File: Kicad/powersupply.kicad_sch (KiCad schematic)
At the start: 26 parts, among them J1101 Jack 2.1{slash}6.3mm, J1102 Conn_02x02, J1103 Conn_01x04, Q1101 SS8050, Q1102 AO3401A, Q1103 SS8550, U1101 DC-DC Module, U1102 LP2950N, U1103 AMS1117-3.3

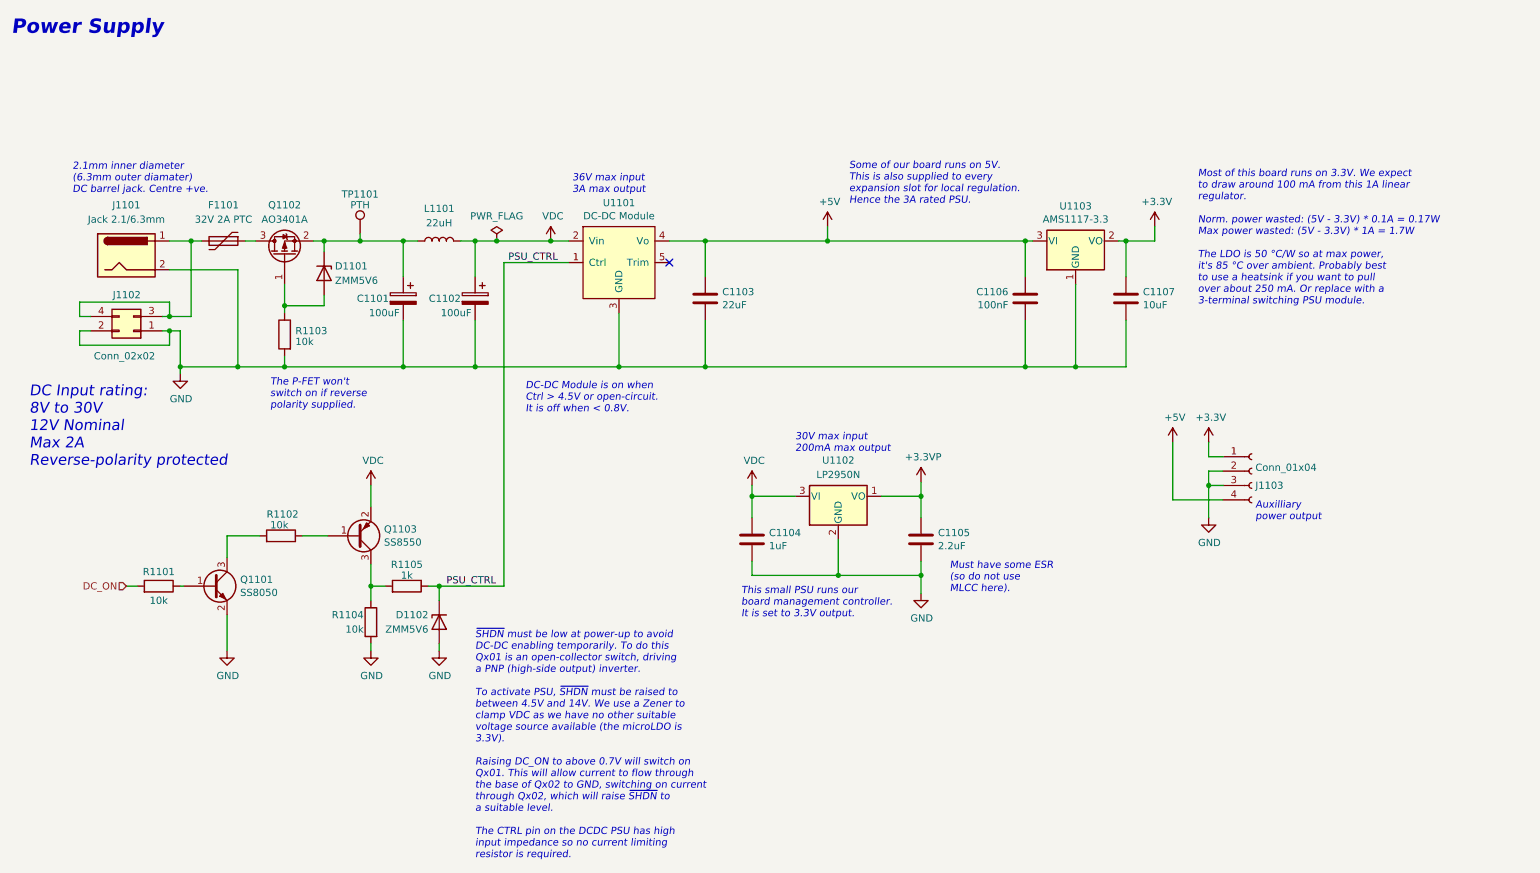
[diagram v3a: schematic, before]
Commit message: Reworked audio circuit.
Based on TLV320AIC23B evaluation board. Removed Pi filters. Used SMD
electrolytic caps for headphone out.
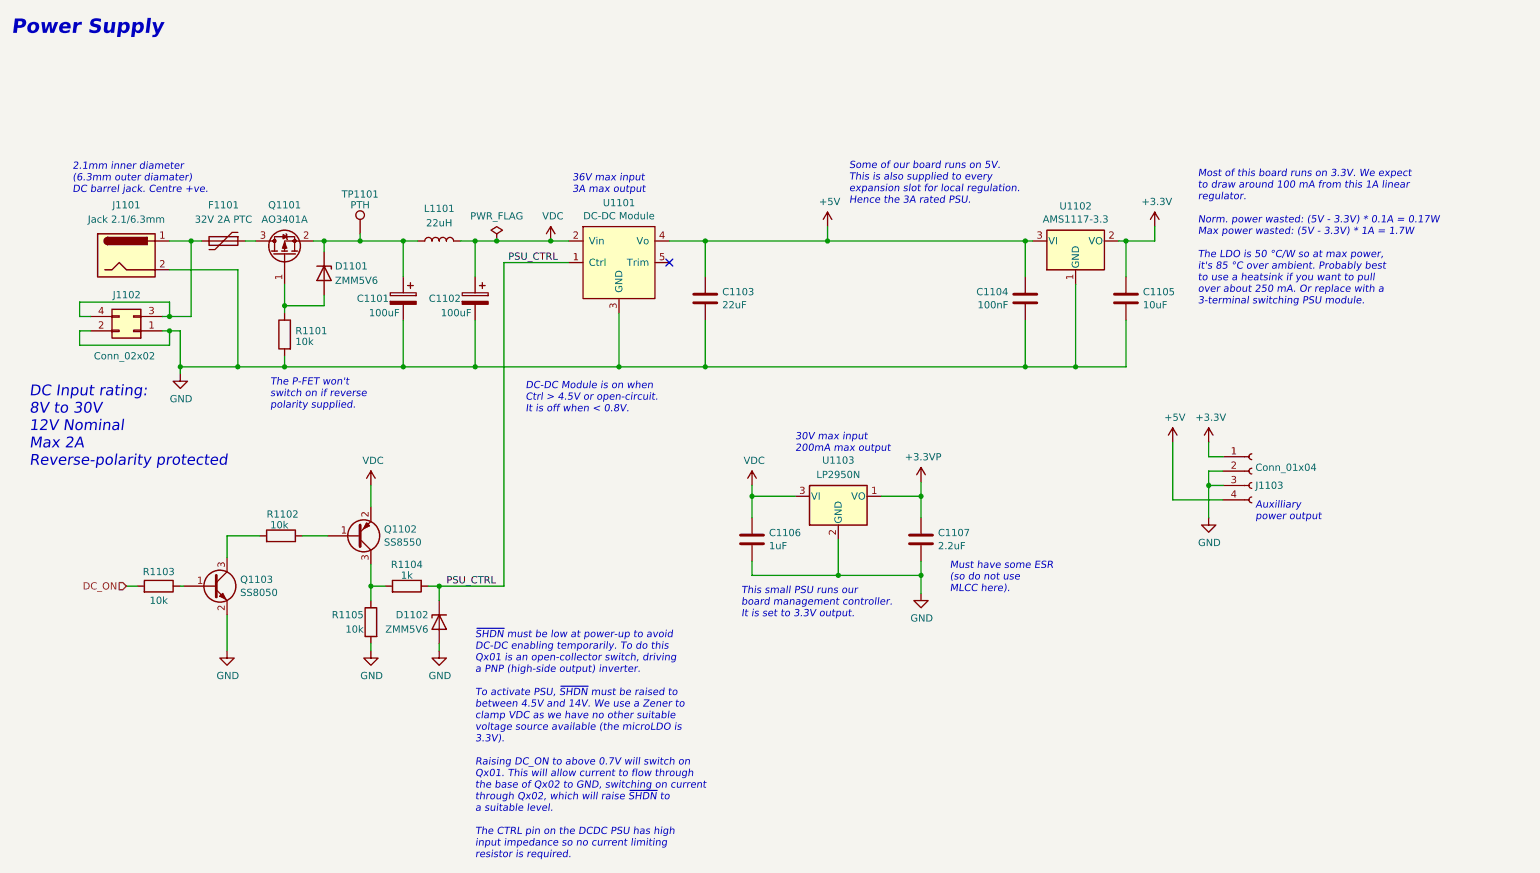
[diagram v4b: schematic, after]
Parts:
- renumbered C1106 to C1104, C1107 to C1105, C1104 to C1106, C1105 to C1107, Q1102 to Q1101, Q1103 to Q1102, Q1101 to Q1103, R1103 to R1101, R1101 to R1103, R1105 to R1104, R1104 to R1105, U1103 to U1102, U1102 to U1103
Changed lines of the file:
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@@
   (symbol (lib_id "Regulator_Linear:AMS1117CD-3.3") (at 200.66 53.975 0) (unit 1)
     (in_bom yes) (on_board yes)
-    (property "Reference" "U1103" (id 0) (at 200.66 47.8282 0))
+    (property "Reference" "U1102" (id 0) (at 200.66 47.8282 0))
     (property "Value" "AMS1117-3.3" (id 1) (at 200.66 50.1396 0))
     (property "Footprint" "Package_TO_SOT_SMD:SOT-223-3_TabPin2" (id 2) (at 200.66 48.895 0)
@@
   (symbol (lib_id "power:GND") (at 42.545 77.47 0) (unit 1)
     (in_bom yes) (on_board yes)
-    (property "Reference" "#PWR01101" (id 0) (at 42.545 83.82 0)
+    (property "Reference" "#PWR01104" (id 0) (at 42.545 83.82 0)
       (effects (font (size 1.27 1.27)) hide)
     )
@@
   (symbol (lib_id "power:+3.3VP") (at 173.355 96.52 0) (unit 1)
     (in_bom yes) (on_board yes)
-    (property "Reference" "#PWR01109" (id 0) (at 177.165 97.79 0)
+    (property "Reference" "#PWR01107" (id 0) (at 177.165 97.79 0)
       (effects (font (size 1.27 1.27)) hide)
     )
@@
   (symbol (lib_id "power:+3.3V") (at 214.63 51.435 0) (unit 1)
     (in_bom yes) (on_board yes)
-    (property "Reference" "#PWR01111" (id 0) (at 214.63 55.245 0)
+    (property "Reference" "#PWR01102" (id 0) (at 214.63 55.245 0)
       (effects (font (size 1.27 1.27)) hide)
     )
@@
   (symbol (lib_id "Device:C") (at 191.77 64.135 0) (mirror y) (unit 1)
     (in_bom yes) (on_board yes)
-    (property "Reference" "C1106" (id 0) (at 188.7728 62.9666 0)
+    (property "Reference" "C1104" (id 0) (at 188.7728 62.9666 0)
       (effects (font (size 1.27 1.27)) (justify left))
     )
@@
   (symbol (lib_id "power:GND") (at 173.355 116.205 0) (unit 1)
     (in_bom yes) (on_board yes)
-    (property "Reference" "#PWR01110" (id 0) (at 173.355 122.555 0)
+    (property "Reference" "#PWR01111" (id 0) (at 173.355 122.555 0)
       (effects (font (size 1.27 1.27)) hide)
     )
@@
   (symbol (lib_id "power:+5V") (at 156.845 51.435 0) (unit 1)
     (in_bom yes) (on_board yes)
-    (property "Reference" "#PWR01108" (id 0) (at 156.845 55.245 0)
+    (property "Reference" "#PWR01101" (id 0) (at 156.845 55.245 0)
       (effects (font (size 1.27 1.27)) hide)
     )
@@
   (symbol (lib_id "Device:R") (at 76.2 121.285 0) (mirror y) (unit 1)
     (in_bom yes) (on_board yes)
-    (property "Reference" "R1104" (id 0) (at 74.93 120.015 0)
+    (property "Reference" "R1105" (id 0) (at 74.93 120.015 0)
       (effects (font (size 1.27 1.27)) (justify left))
     )
@@
   (symbol (lib_id "power:VDC") (at 107.95 53.975 0) (unit 1)
     (in_bom yes) (on_board yes)
-    (property "Reference" "#PWR01106" (id 0) (at 107.95 56.515 0)
+    (property "Reference" "#PWR01103" (id 0) (at 107.95 56.515 0)
       (effects (font (size 1.27 1.27)) hide)
     )
@@
   (symbol (lib_id "power:VDC") (at 76.2 97.155 0) (unit 1)
     (in_bom yes) (on_board yes)
-    (property "Reference" "#PWR01103" (id 0) (at 76.2 99.695 0)
+    (property "Reference" "#PWR01108" (id 0) (at 76.2 99.695 0)
       (effects (font (size 1.27 1.27)) hide)
     )
@@
   (symbol (lib_id "Transistor_BJT:BC817") (at 48.26 114.935 0) (unit 1)
     (in_bom yes) (on_board yes)
-    (property "Reference" "Q1101" (id 0) (at 53.1114 113.7666 0)
+    (property "Reference" "Q1103" (id 0) (at 53.1114 113.7666 0)
       (effects (font (size 1.27 1.27)) (justify left))
     )
@@
   (symbol (lib_id "power:GND") (at 76.2 126.365 0) (unit 1)
     (in_bom yes) (on_board yes)
-    (property "Reference" "#PWR01104" (id 0) (at 76.2 132.715 0)
+    (property "Reference" "#PWR01113" (id 0) (at 76.2 132.715 0)
       (effects (font (size 1.27 1.27)) hide)
     )
@@
   (symbol (lib_id "Transistor_BJT:BC807") (at 73.66 106.045 0) (mirror x) (unit 1)
     (in_bom yes) (on_board yes)
-    (property "Reference" "Q1103" (id 0) (at 78.5114 104.8766 0)
+    (property "Reference" "Q1102" (id 0) (at 78.5114 104.8766 0)
       (effects (font (size 1.27 1.27)) (justify left))
     )
@@
   (symbol (lib_id "power:GND") (at 50.8 126.365 0) (unit 1)
     (in_bom yes) (on_board yes)
-    (property "Reference" "#PWR01102" (id 0) (at 50.8 132.715 0)
+    (property "Reference" "#PWR01112" (id 0) (at 50.8 132.715 0)
       (effects (font (size 1.27 1.27)) hide)
     )
@@
   (symbol (lib_id "Device:R") (at 38.735 114.935 270) (mirror x) (unit 1)
     (in_bom yes) (on_board yes)
-    (property "Reference" "R1101" (id 0) (at 38.735 112.395 90))
+    (property "Reference" "R1103" (id 0) (at 38.735 112.395 90))
     (property "Value" "10k" (id 1) (at 38.735 117.475 90))
     (property "Footprint" "Resistor_SMD:R_0805_2012Metric_Pad1.20x1.40mm_HandSolder" (id 2) (at 38.735 116.713 90)
@@
   (symbol (lib_id "power:GND") (at 224.155 102.87 0) (unit 1)
     (in_bom yes) (on_board yes)
-    (property "Reference" "#PWR01114" (id 0) (at 224.155 109.22 0)
+    (property "Reference" "#PWR01110" (id 0) (at 224.155 109.22 0)
       (effects (font (size 1.27 1.27)) hide)
     )
@@
   (symbol (lib_id "power:+5V") (at 217.805 89.535 0) (unit 1)
     (in_bom yes) (on_board yes)
-    (property "Reference" "#PWR01112" (id 0) (at 217.805 93.345 0)
+    (property "Reference" "#PWR01105" (id 0) (at 217.805 93.345 0)
       (effects (font (size 1.27 1.27)) hide)
     )
@@
   (symbol (lib_id "Device:R") (at 82.55 114.935 270) (mirror x) (unit 1)
     (in_bom yes) (on_board yes)
-    (property "Reference" "R1105" (id 0) (at 82.55 111.125 90))
+    (property "Reference" "R1104" (id 0) (at 82.55 111.125 90))
     (property "Value" "1k" (id 1) (at 82.55 113.03 90))
     (property "Footprint" "Resistor_SMD:R_0805_2012Metric_Pad1.20x1.40mm_HandSolder" (id 2) (at 82.55 116.713 90)
@@
   (symbol (lib_id "power:GND") (at 88.265 126.365 0) (unit 1)
     (in_bom yes) (on_board yes)
-    (property "Reference" "#PWR01105" (id 0) (at 88.265 132.715 0)
+    (property "Reference" "#PWR01114" (id 0) (at 88.265 132.715 0)
       (effects (font (size 1.27 1.27)) hide)
     )
@@
   (symbol (lib_id "power:+3.3V") (at 224.155 89.535 0) (unit 1)
     (in_bom yes) (on_board yes)
-    (property "Reference" "#PWR01113" (id 0) (at 224.155 93.345 0)
+    (property "Reference" "#PWR01106" (id 0) (at 224.155 93.345 0)
       (effects (font (size 1.27 1.27)) hide)
     )
@@
   (symbol (lib_id "Device:C") (at 173.355 106.68 0) (unit 1)
     (in_bom yes) (on_board yes)
-    (property "Reference" "C1105" (id 0) (at 176.3522 105.5116 0)
+    (property "Reference" "C1107" (id 0) (at 176.3522 105.5116 0)
       (effects (font (size 1.27 1.27)) (justify left))
     )
@@
   (symbol (lib_id "Regulator_Linear:LP2950-3.3_TO92") (at 158.75 99.06 0) (unit 1)
     (in_bom yes) (on_board yes)
-    (property "Reference" "U1102" (id 0) (at 158.75 92.71 0))
+    (property "Reference" "U1103" (id 0) (at 158.75 92.71 0))
     (property "Value" "LP2950N" (id 1) (at 158.75 95.25 0))
     (property "Footprint" "Package_TO_SOT_THT:TO-92_Inline" (id 2) (at 158.75 93.345 0)
@@
   (symbol (lib_id "Device:C") (at 143.51 106.68 0) (unit 1)
     (in_bom yes) (on_board yes)
-    (property "Reference" "C1104" (id 0) (at 146.5072 105.5116 0)
+    (property "Reference" "C1106" (id 0) (at 146.5072 105.5116 0)
       (effects (font (size 1.27 1.27)) (justify left))
     )
@@
   (symbol (lib_id "Device:R") (at 60.96 70.485 0) (mirror y) (unit 1)
     (in_bom yes) (on_board yes)
-    (property "Reference" "R1103" (id 0) (at 62.865 69.85 0)
+    (property "Reference" "R1101" (id 0) (at 62.865 69.85 0)
       (effects (font (size 1.27 1.27)) (justify right))
     )
@@
   (symbol (lib_id "Device:C") (at 209.55 64.135 0) (unit 1)
     (in_bom yes) (on_board yes)
-    (property "Reference" "C1107" (id 0) (at 212.5472 62.9666 0)
+    (property "Reference" "C1105" (id 0) (at 212.5472 62.9666 0)
       (effects (font (size 1.27 1.27)) (justify left))
     )
@@
   (symbol (lib_id "Transistor_FET:AO3401A") (at 60.96 56.515 90) (unit 1)
     (in_bom yes) (on_board yes)
-    (property "Reference" "Q1102" (id 0) (at 60.96 47.625 90))
+    (property "Reference" "Q1101" (id 0) (at 60.96 47.625 90))
     (property "Value" "AO3401A" (id 1) (at 60.96 50.165 90))
     (property "Footprint" "Package_TO_SOT_SMD:SOT-23" (id 2) (at 62.865 51.435 0)
@@
   (symbol (lib_id "power:VDC") (at 143.51 97.155 0) (unit 1)
     (in_bom yes) (on_board yes)
-    (property "Reference" "#PWR01107" (id 0) (at 143.51 99.695 0)
-      (effects (font (size 1.27 1.27)) hide)
-    )
+    (property "Reference" "#PWR01109" (id 0) (at 143.51 99.695 0)
+      (effects (font (size 1.27 1.27)) hide)
+    )

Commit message: Added a PC Speaker output.
To free up a BMC pin, the HDD LED is now driven from the I/O mux.
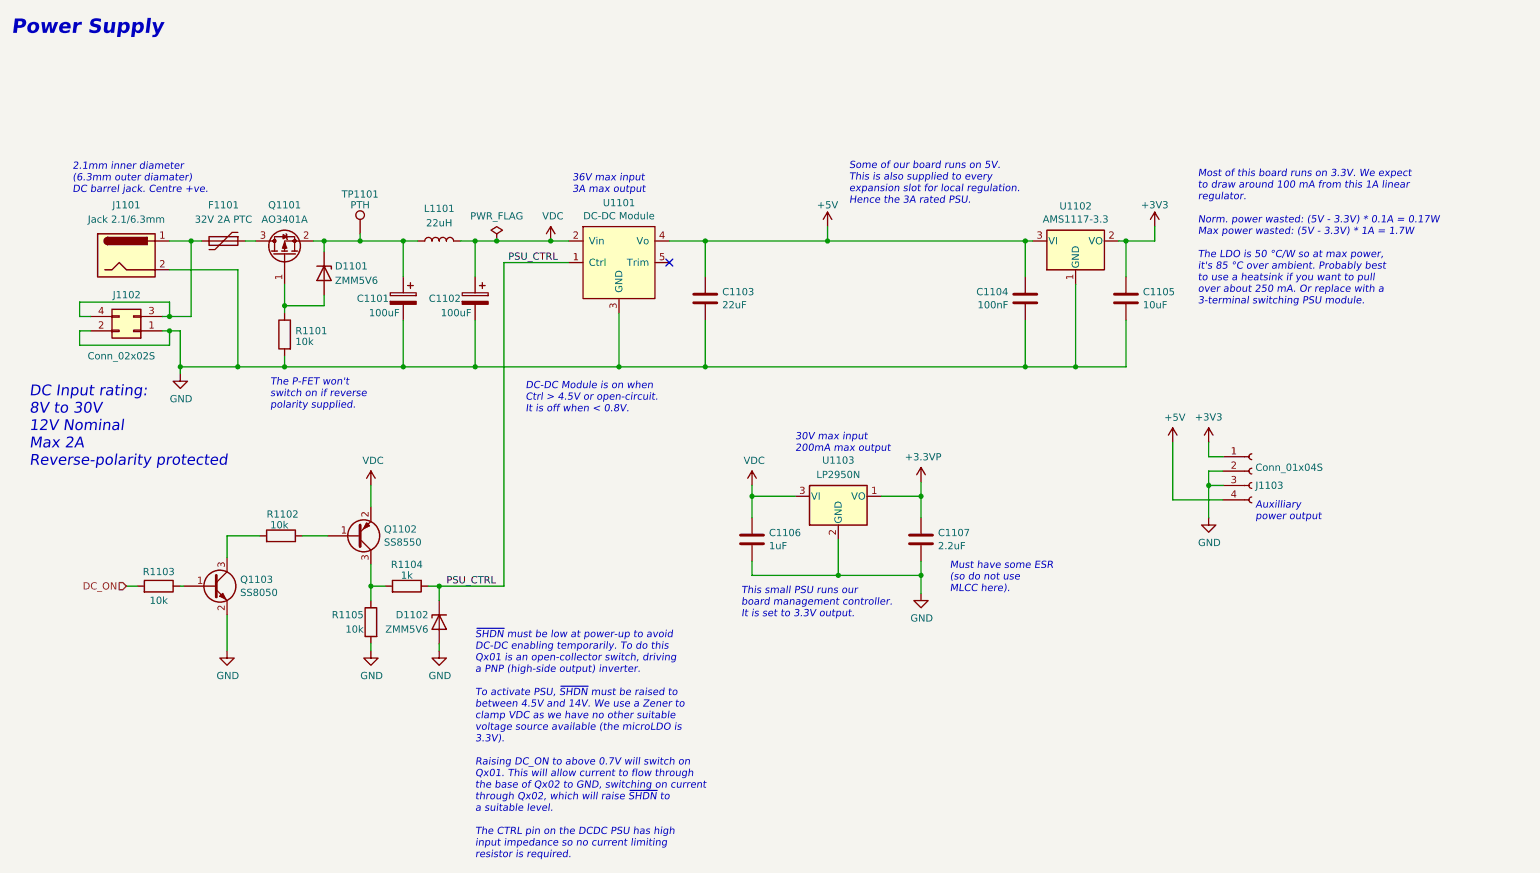
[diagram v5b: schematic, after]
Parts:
- J1102: value Conn_02x02 -> Conn_02x02S
- J1103: value Conn_01x04 -> Conn_01x04S
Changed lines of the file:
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@@
     (pin "2")
-  )
-  (symbol (lib_id "power:+3.3V") (at 214.63 51.435 0) (unit 1)
-    (in_bom yes) (on_board yes)
-    (property "Reference" "#PWR01102" (id 0) (at 214.63 55.245 0)
-      (effects (font (size 1.27 1.27)) hide)
-    )
-    (property "Value" "+3.3V" (id 1) (at 215.011 47.0408 0))
-    (property "Footprint" "" (id 2) (at 214.63 51.435 0)
-      (effects (font (size 1.27 1.27)) hide)
-    )
-    (property "Datasheet" "" (id 3) (at 214.63 51.435 0)
-      (effects (font (size 1.27 1.27)) hide)
-    )
-    (pin "1")
   )
   (symbol (lib_id "Device:C") (at 191.77 64.135 0) (mirror y) (unit 1)
@@
       (effects (font (size 1.27 1.27)) hide)
     )
-    (property "Value" "+5V" (id 1) (at 157.226 47.0408 0))
+    (property "Value" "+5V" (id 1) (at 156.845 47.625 0))
     (property "Footprint" "" (id 2) (at 156.845 51.435 0)
       (effects (font (size 1.27 1.27)) hide)
@@
       (effects (font (size 1.27 1.27)) (justify left))
     )
-    (property "Value" "Conn_01x04" (id 1) (at 232.41 93.98 0)
+    (property "Value" "Conn_01x04S" (id 1) (at 232.41 93.98 0)
       (effects (font (size 1.27 1.27)) (justify left))
     )
@@
     )
     (property "Datasheet" "" (id 3) (at 217.805 89.535 0)
+      (effects (font (size 1.27 1.27)) hide)
+    )
+    (pin "1")
+  )
+  (symbol (lib_id "power:+3V3") (at 214.63 51.435 0) (unit 1)
+    (in_bom yes) (on_board yes)
+    (property "Reference" "#PWR01102" (id 0) (at 214.63 55.245 0)
+      (effects (font (size 1.27 1.27)) hide)
+    )
+    (property "Value" "+3V3" (id 1) (at 214.63 47.625 0))
+    (property "Footprint" "" (id 2) (at 214.63 51.435 0)
+      (effects (font (size 1.27 1.27)) hide)
+    )
+    (property "Datasheet" "" (id 3) (at 214.63 51.435 0)
       (effects (font (size 1.27 1.27)) hide)
     )
@@
       (effects (font (size 1.27 1.27)) (justify left))
     )
-    (property "Value" "Conn_02x02" (id 1) (at 38.1 74.295 0)
+    (property "Value" "Conn_02x02S" (id 1) (at 38.1 74.295 0)
       (effects (font (size 1.27 1.27)) (justify left))
     )
@@
     (pin "1")
     (pin "2")
-  )
-  (symbol (lib_id "power:+3.3V") (at 224.155 89.535 0) (unit 1)
-    (in_bom yes) (on_board yes)
-    (property "Reference" "#PWR01106" (id 0) (at 224.155 93.345 0)
-      (effects (font (size 1.27 1.27)) hide)
-    )
-    (property "Value" "+3.3V" (id 1) (at 224.536 85.1408 0))
-    (property "Footprint" "" (id 2) (at 224.155 89.535 0)
-      (effects (font (size 1.27 1.27)) hide)
-    )
-    (property "Datasheet" "" (id 3) (at 224.155 89.535 0)
-      (effects (font (size 1.27 1.27)) hide)
-    )
-    (pin "1")
   )
   (symbol (lib_id "Device:C") (at 173.355 106.68 0) (unit 1)
@@
     (pin "2")
   )
+  (symbol (lib_id "power:+3V3") (at 224.155 89.535 0) (unit 1)
+    (in_bom yes) (on_board yes)
+    (property "Reference" "#PWR01106" (id 0) (at 224.155 93.345 0)
+      (effects (font (size 1.27 1.27)) hide)
+    )
+    (property "Value" "+3V3" (id 1) (at 224.155 85.09 0))
+    (property "Footprint" "" (id 2) (at 224.155 89.535 0)
+      (effects (font (size 1.27 1.27)) hide)
+    )
+    (property "Datasheet" "" (id 3) (at 224.155 89.535 0)
+      (effects (font (size 1.27 1.27)) hide)
+    )
+    (pin "1")
+  )
   (symbol (lib_id "Device:C") (at 209.55 64.135 0) (unit 1)
